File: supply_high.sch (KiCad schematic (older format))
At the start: 41 parts

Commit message: - final schematic
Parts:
- gave numbers to parts that had none: 41
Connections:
- net HVGND: now also C191.2, C192.1; no longer C191.1, C192.2
- net at C193.1, C194.1, D38.2 (A)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: now also C191.1, C192.2; no longer C191.2, C192.1
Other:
- moved on the sheet: C191, C192

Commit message: - init PCB - fix last things in schematic
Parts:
- U38: footprint (none) -> Package_SO:SOP-8_3.9x4.9mm_P1.27mm
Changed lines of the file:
@@
 F 0 "U38" H 4250 5567 50  0000 C CNN
 F 1 "TC7660S" H 4250 5476 50  0000 C CNN
-F 2 "" H 4350 5050 50  0001 C CNN
+F 2 "Package_SO:SOP-8_3.9x4.9mm_P1.27mm" H 4350 5050 50  0001 C CNN
 F 3 "http://datasheets.maximintegrated.com/en/ds/ICL7660-MAX1044.pdf" H 4350 5050 50  0001 C CNN
 	1    4250 5150
@@
 Wire Wire Line
 	5150 4750 4850 4750
+$Comp
+L power:PWR_FLAG #FLG?
+U 1 1 5FA95447
+P 3400 4600
+AR Path="/5F61C123/5FA95447" Ref="#FLG?"  Part="1"
+AR Path="/5FB035A9/5FA95447" Ref="#FLG0111"  Part="1"
+F 0 "#FLG0111" H 3400 4675 50  0001 C CNN
+F 1 "PWR_FLAG" H 3400 4774 50  0001 C CNN
+F 2 "" H 3400 4600 50  0001 C CNN
+F 3 "~" H 3400 4600 50  0001 C CNN
+	1    3400 4600
+	1    0    0    -1
+$EndComp
 $EndSCHEMATC

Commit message: - PCB progress
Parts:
- C177, C179, C181, C182, C183, C185, C186, C187, C188, C189, C190, C191, C194, C195, C197: footprint Capacitor_SMD:C_0603_1608Metric_Pad1.05x0.95mm_HandSolder -> Capacitor_SMD:C_0603_1608Metric
- C178, C180, C193, C196: footprint Capacitor_SMD:C_0805_2012Metric_Pad1.15x1.40mm_HandSolder -> Capacitor_SMD:C_0805_2012Metric
- C184, C192, C198: footprint Capacitor_SMD:C_0805_2012Metric_Pad1.15x1.40mm_HandSolder -> Capacitor_SMD:C_0603_1608Metric_Pad1.05x0.95mm_HandSolder
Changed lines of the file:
@@
 F 0 "C188" H 3400 4650 50  0000 R BNN
 F 1 "100n" H 3400 4850 50  0000 R TNN
-F 2 "Capacitor_SMD:C_0603_1608Metric_Pad1.05x0.95mm_HandSolder" H 3400 4750 50  0001 C CNN
+F 2 "Capacitor_SMD:C_0603_1608Metric" H 3400 4750 50  0001 C CNN
 F 3 "~" H 3400 4750 50  0001 C CNN
 	1    3400 4750
@@
 F 0 "C183" H 6850 2750 50  0000 L BNN
 F 1 "10n" H 6850 2650 50  0000 L TNN
-F 2 "Capacitor_SMD:C_0603_1608Metric_Pad1.05x0.95mm_HandSolder" H 6800 2700 50  0001 C CNN
+F 2 "Capacitor_SMD:C_0603_1608Metric" H 6800 2700 50  0001 C CNN
 F 3 "~" H 6800 2700 50  0001 C CNN
 	1    6800 2700
@@
 F 0 "C182" H 5800 2750 50  0000 L BNN
 F 1 "100n" H 5800 2650 50  0000 L TNN
-F 2 "Capacitor_SMD:C_0603_1608Metric_Pad1.05x0.95mm_HandSolder" H 5750 2700 50  0001 C CNN
+F 2 "Capacitor_SMD:C_0603_1608Metric" H 5750 2700 50  0001 C CNN
 F 3 "~" H 5750 2700 50  0001 C CNN
 	1    5750 2700
@@
 F 0 "C181" H 5500 2750 50  0000 L BNN
 F 1 "1u" H 5500 2650 50  0000 L TNN
-F 2 "Capacitor_SMD:C_0603_1608Metric_Pad1.05x0.95mm_HandSolder" H 5450 2700 50  0001 C CNN
+F 2 "Capacitor_SMD:C_0603_1608Metric" H 5450 2700 50  0001 C CNN
 F 3 "~" H 5450 2700 50  0001 C CNN
 	1    5450 2700
@@
 F 0 "C184" H 7150 2750 50  0000 L BNN
 F 1 "10u" H 7150 2650 50  0000 L TNN
-F 2 "Capacitor_SMD:C_0805_2012Metric_Pad1.15x1.40mm_HandSolder" H 7100 2700 50  0001 C CNN
+F 2 "Capacitor_SMD:C_0603_1608Metric_Pad1.05x0.95mm_HandSolder" H 7100 2700 50  0001 C CNN
 F 3 "Samsung CL21A106KQFNNNE" H 7100 2700 50  0001 C CNN
 	1    7100 2700
@@
 F 0 "C186" H 7750 2750 50  0000 L BNN
 F 1 "100n" H 7750 2650 50  0000 L TNN
-F 2 "Capacitor_SMD:C_0603_1608Metric_Pad1.05x0.95mm_HandSolder" H 7700 2700 50  0001 C CNN
+F 2 "Capacitor_SMD:C_0603_1608Metric" H 7700 2700 50  0001 C CNN
 F 3 "~" H 7700 2700 50  0001 C CNN
 	1    7700 2700
@@
 F 0 "C185" H 7450 2750 50  0000 L BNN
 F 1 "1u" H 7450 2650 50  0000 L TNN
-F 2 "Capacitor_SMD:C_0603_1608Metric_Pad1.05x0.95mm_HandSolder" H 7400 2700 50  0001 C CNN
+F 2 "Capacitor_SMD:C_0603_1608Metric" H 7400 2700 50  0001 C CNN
 F 3 "~" H 7400 2700 50  0001 C CNN
 	1    7400 2700
@@
 F 0 "C198" H 3650 5300 50  0000 L BNN
 F 1 "10u" H 3650 5200 50  0000 L TNN
-F 2 "Capacitor_SMD:C_0805_2012Metric_Pad1.15x1.40mm_HandSolder" H 3600 5250 50  0001 C CNN
+F 2 "Capacitor_SMD:C_0603_1608Metric_Pad1.05x0.95mm_HandSolder" H 3600 5250 50  0001 C CNN
 F 3 "Samsung CL21A106KQFNNNE" H 3600 5250 50  0001 C CNN
 	1    3600 5250
@@
 F 0 "C197" H 3350 5300 50  0000 L BNN
 F 1 "100n" H 3350 5200 50  0000 L TNN
-F 2 "Capacitor_SMD:C_0603_1608Metric_Pad1.05x0.95mm_HandSolder" H 3300 5250 50  0001 C CNN
+F 2 "Capacitor_SMD:C_0603_1608Metric" H 3300 5250 50  0001 C CNN
 F 3 "~" H 3300 5250 50  0001 C CNN
 	1    3300 5250
@@
 F 0 "C192" H 5500 5000 50  0000 L BNN
 F 1 "10u" H 5500 4900 50  0000 L TNN
-F 2 "Capacitor_SMD:C_0805_2012Metric_Pad1.15x1.40mm_HandSolder" H 5450 4950 50  0001 C CNN
+F 2 "Capacitor_SMD:C_0603_1608Metric_Pad1.05x0.95mm_HandSolder" H 5450 4950 50  0001 C CNN
 F 3 "Samsung CL21A106KQFNNNE" H 5450 4950 50  0001 C CNN
 	1    5450 4950
@@
 F 0 "C190" H 4850 4850 50  0000 R BNN
 F 1 "100n" H 4850 5050 50  0000 R TNN
-F 2 "Capacitor_SMD:C_0603_1608Metric_Pad1.05x0.95mm_HandSolder" H 4850 4950 50  0001 C CNN
+F 2 "Capacitor_SMD:C_0603_1608Metric" H 4850 4950 50  0001 C CNN
 F 3 "~" H 4850 4950 50  0001 C CNN
 	1    4850 4950
@@
 F 0 "C191" H 5150 4850 50  0000 R BNN
 F 1 "100n" H 5150 5050 50  0000 R TNN
-F 2 "Capacitor_SMD:C_0603_1608Metric_Pad1.05x0.95mm_HandSolder" H 5150 4950 50  0001 C CNN
+F 2 "Capacitor_SMD:C_0603_1608Metric" H 5150 4950 50  0001 C CNN
 F 3 "~" H 5150 4950 50  0001 C CNN
 	1    5150 4950
@@
 F 0 "C193" H 5900 5050 50  0000 L BNN
 F 1 "2u2" H 5900 4950 50  0000 L TNN
-F 2 "Capacitor_SMD:C_0805_2012Metric_Pad1.15x1.40mm_HandSolder" H 5850 5000 50  0001 C CNN
+F 2 "Capacitor_SMD:C_0805_2012Metric" H 5850 5000 50  0001 C CNN
 F 3 "~" H 5850 5000 50  0001 C CNN
 	1    5850 5000
@@
 F 0 "C194" H 6250 5050 50  0000 L BNN
 F 1 "100n" H 6250 4950 50  0000 L TNN
-F 2 "Capacitor_SMD:C_0603_1608Metric_Pad1.05x0.95mm_HandSolder" H 6200 5000 50  0001 C CNN
+F 2 "Capacitor_SMD:C_0603_1608Metric" H 6200 5000 50  0001 C CNN
 F 3 "~" H 6200 5000 50  0001 C CNN
 	1    6200 5000
@@
 F 0 "C196" H 8250 5050 50  0000 L BNN
 F 1 "2u2" H 8250 4950 50  0000 L TNN
-F 2 "Capacitor_SMD:C_0805_2012Metric_Pad1.15x1.40mm_HandSolder" H 8200 5000 50  0001 C CNN
+F 2 "Capacitor_SMD:C_0805_2012Metric" H 8200 5000 50  0001 C CNN
 F 3 "~" H 8200 5000 50  0001 C CNN
 	1    8200 5000
@@
 F 0 "C195" H 7900 5050 50  0000 L BNN
 F 1 "100n" H 7900 4950 50  0000 L TNN
-F 2 "Capacitor_SMD:C_0603_1608Metric_Pad1.05x0.95mm_HandSolder" H 7850 5000 50  0001 C CNN
+F 2 "Capacitor_SMD:C_0603_1608Metric" H 7850 5000 50  0001 C CNN
 F 3 "~" H 7850 5000 50  0001 C CNN
 	1    7850 5000
@@
 F 0 "C189" H 7050 4900 50  0000 L BNN
 F 1 "1u" H 7050 4800 50  0000 L TNN
-F 2 "Capacitor_SMD:C_0603_1608Metric_Pad1.05x0.95mm_HandSolder" H 7000 4850 50  0001 C CNN
+F 2 "Capacitor_SMD:C_0603_1608Metric" H 7000 4850 50  0001 C CNN
 F 3 "~" H 7000 4850 50  0001 C CNN
 	1    7000 4850
@@
 F 0 "C180" H 4850 2750 50  0000 L BNN
 F 1 "2u2" H 4850 2650 50  0000 L TNN
-F 2 "Capacitor_SMD:C_0805_2012Metric_Pad1.15x1.40mm_HandSolder" H 4800 2700 50  0001 C CNN
+F 2 "Capacitor_SMD:C_0805_2012Metric" H 4800 2700 50  0001 C CNN
 F 3 "~" H 4800 2700 50  0001 C CNN
 	1    4800 2700
@@
 F 0 "C179" H 4500 2750 50  0000 L BNN
 F 1 "100n" H 4500 2650 50  0000 L TNN
-F 2 "Capacitor_SMD:C_0603_1608Metric_Pad1.05x0.95mm_HandSolder" H 4450 2700 50  0001 C CNN
+F 2 "Capacitor_SMD:C_0603_1608Metric" H 4450 2700 50  0001 C CNN
 F 3 "~" H 4450 2700 50  0001 C CNN
 	1    4450 2700
@@
 F 0 "C187" H 3850 3000 50  0000 L BNN
 F 1 "1u" H 3850 2900 50  0000 L TNN
-F 2 "Capacitor_SMD:C_0603_1608Metric_Pad1.05x0.95mm_HandSolder" H 3800 2950 50  0001 C CNN
+F 2 "Capacitor_SMD:C_0603_1608Metric" H 3800 2950 50  0001 C CNN
 F 3 "~" H 3800 2950 50  0001 C CNN
 	1    3800 2950
@@
 F 0 "C178" H 3000 2750 50  0000 L BNN
 F 1 "2u2" H 3000 2650 50  0000 L TNN
-F 2 "Capacitor_SMD:C_0805_2012Metric_Pad1.15x1.40mm_HandSolder" H 2950 2700 50  0001 C CNN
+F 2 "Capacitor_SMD:C_0805_2012Metric" H 2950 2700 50  0001 C CNN
 F 3 "~" H 2950 2700 50  0001 C CNN
 	1    2950 2700
@@
 F 0 "C177" H 2700 2750 50  0000 L BNN
 F 1 "100n" H 2700 2650 50  0000 L TNN
-F 2 "Capacitor_SMD:C_0603_1608Metric_Pad1.05x0.95mm_HandSolder" H 2650 2700 50  0001 C CNN
+F 2 "Capacitor_SMD:C_0603_1608Metric" H 2650 2700 50  0001 C CNN
 F 3 "~" H 2650 2700 50  0001 C CNN
 	1    2650 2700

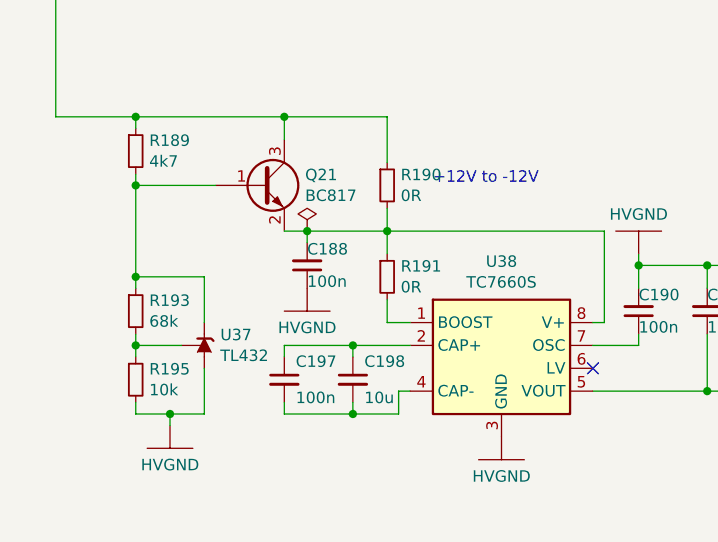
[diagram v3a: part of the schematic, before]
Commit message: - PCB WiP - Pump output aligned
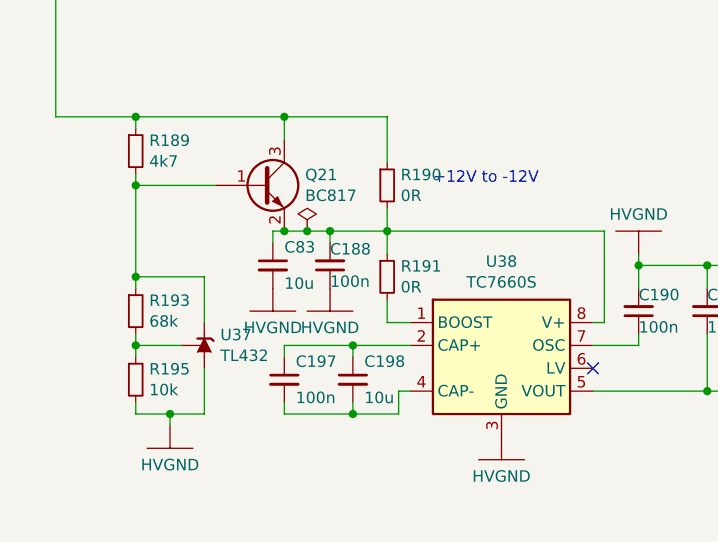
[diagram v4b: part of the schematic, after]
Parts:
- added C83: 10u, Capacitor_SMD:C_0603_1608Metric_Pad1.05x0.95mm_HandSolder, symbol Device:C_Small
- R189, R190, R191: footprint Resistor_SMD:R_0603_1608Metric_Pad1.05x0.95mm_HandSolder -> Resistor_SMD:R_0603_1608Metric
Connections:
- net HVGND: now also C83.2
- net at C188.2, Q21.2 (E), R190.2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: now also C83.1
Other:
- moved on the sheet: C188
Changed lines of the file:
@@
 L Device:C_Small C?
 U 1 1 5FB2240D
-P 3400 4750
+P 3500 4750
 AR Path="/5F40DCB9/5FB2240D" Ref="C?"  Part="1"
 AR Path="/5F463F4C/5FB2240D" Ref="C?"  Part="1"
@@
 AR Path="/5F61C123/5FB2240D" Ref="C?"  Part="1"
 AR Path="/5FB035A9/5FB2240D" Ref="C188"  Part="1"
-F 0 "C188" H 3400 4650 50  0000 R BNN
-F 1 "100n" H 3400 4850 50  0000 R TNN
-F 2 "Capacitor_SMD:C_0603_1608Metric" H 3400 4750 50  0001 C CNN
-F 3 "~" H 3400 4750 50  0001 C CNN
-	1    3400 4750
+F 0 "C188" H 3500 4650 50  0000 R BNN
+F 1 "100n" H 3500 4850 50  0000 R TNN
+F 2 "Capacitor_SMD:C_0603_1608Metric" H 3500 4750 50  0001 C CNN
+F 3 "~" H 3500 4750 50  0001 C CNN
+	1    3500 4750
 	-1   0    0    1
 $EndComp
@@
 F 0 "R191" H 3809 4846 50  0000 L CNN
 F 1 "0R" H 3809 4755 50  0000 L CNN
-F 2 "Resistor_SMD:R_0603_1608Metric_Pad1.05x0.95mm_HandSolder" H 3750 4800 50  0001 C CNN
+F 2 "Resistor_SMD:R_0603_1608Metric" H 3750 4800 50  0001 C CNN
 F 3 "~" H 3750 4800 50  0001 C CNN
 	1    3750 4800
@@
 F 0 "R189" H 2709 4296 50  0000 L CNN
 F 1 "4k7" H 2709 4205 50  0000 L CNN
-F 2 "Resistor_SMD:R_0603_1608Metric_Pad1.05x0.95mm_HandSolder" H 2650 4250 50  0001 C CNN
+F 2 "Resistor_SMD:R_0603_1608Metric" H 2650 4250 50  0001 C CNN
 F 3 "~" H 2650 4250 50  0001 C CNN
 	1    2650 4250
@@
 F 0 "R190" H 3809 4446 50  0000 L CNN
 F 1 "0R" H 3809 4355 50  0000 L CNN
-F 2 "Resistor_SMD:R_0603_1608Metric_Pad1.05x0.95mm_HandSolder" H 3750 4400 50  0001 C CNN
+F 2 "Resistor_SMD:R_0603_1608Metric" H 3750 4400 50  0001 C CNN
 F 3 "~" H 3750 4400 50  0001 C CNN
 	1    3750 4400
@@
 L power_my:HVGND #PWR?
 U 1 1 5FB44224
-P 3400 4850
+P 3500 4850
 AR Path="/5FB44224" Ref="#PWR?"  Part="1"
 AR Path="/5FB035A9/5FB44224" Ref="#PWR0244"  Part="1"
-F 0 "#PWR0244" H 3400 4800 50  0001 C CNN
-F 1 "HVGND" H 3400 4677 50  0000 C CNN
-F 2 "" H 3400 4850 50  0001 C CNN
-F 3 "" H 3400 4850 50  0001 C CNN
-	1    3400 4850
-	1    0    0    -1
-$EndComp
-Wire Wire Line
-	3750 4600 3400 4600
+F 0 "#PWR0244" H 3500 4800 50  0001 C CNN
+F 1 "HVGND" H 3500 4677 50  0000 C CNN
+F 2 "" H 3500 4850 50  0001 C CNN
+F 3 "" H 3500 4850 50  0001 C CNN
+	1    3500 4850
+	1    0    0    -1
+$EndComp
+Wire Wire Line
+	3750 4600 3500 4600
 Connection ~ 3750 4600
-Wire Wire Line
-	3400 4650 3400 4600
 Connection ~ 3400 4600
 Wire Wire Line
@@
 	1    0    0    -1
 $EndComp
+$Comp
+L Device:C_Small C?
+U 1 1 5FAA7ACF
+P 3250 4750
+AR Path="/5F620813/5FAA7ACF" Ref="C?"  Part="1"
+AR Path="/5F7A93EE/5FAA7ACF" Ref="C?"  Part="1"
+AR Path="/5FB035A9/5FAA7ACF" Ref="C83"  Part="1"
+F 0 "C83" H 3300 4800 50  0000 L BNN
+F 1 "10u" H 3300 4700 50  0000 L TNN
+F 2 "Capacitor_SMD:C_0603_1608Metric_Pad1.05x0.95mm_HandSolder" H 3250 4750 50  0001 C CNN
+F 3 "Samsung CL21A106KQFNNNE" H 3250 4750 50  0001 C CNN
+	1    3250 4750
+	1    0    0    -1
+$EndComp
+$Comp
+L power_my:HVGND #PWR?
+U 1 1 5FAADF04
+P 3250 4850
+AR Path="/5FAADF04" Ref="#PWR?"  Part="1"
+AR Path="/5FB035A9/5FAADF04" Ref="#PWR087"  Part="1"
+F 0 "#PWR087" H 3250 4800 50  0001 C CNN
+F 1 "HVGND" H 3250 4677 50  0000 C CNN
+F 2 "" H 3250 4850 50  0001 C CNN
+F 3 "" H 3250 4850 50  0001 C CNN
+	1    3250 4850
+	1    0    0    -1
+$EndComp
+Wire Wire Line
+	3250 4650 3250 4600
+Wire Wire Line
+	3250 4600 3300 4600
+Connection ~ 3300 4600
+Wire Wire Line
+	3500 4650 3500 4600
+Connection ~ 3500 4600
+Wire Wire Line
+	3500 4600 3400 4600
 $EndSCHEMATC

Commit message: - PCB WiP
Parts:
- removed C186: 100n, Capacitor_SMD:C_0603_1608Metric, symbol Device:C_Small
- removed C193: 2u2, Capacitor_SMD:C_0805_2012Metric, symbol Device:C_Small
- added D13: 1N4448, miscellaneous_my:D_SOD-323-523_HandSoldering, symbol Device:D_Small
- D35, D36, D37, D38: footprint Diode_SMD:D_SOD-323_HandSoldering -> miscellaneous_my:D_SOD-323-523_HandSoldering
- U38: footprint Package_SO:SOP-8_3.9x4.9mm_P1.27mm -> Package_SO:SOIC-8_3.9x4.9mm_P1.27mm
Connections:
- net HV+3V3: now also D13.2 (A)
- net HV+5V: now also D13.1 (K)
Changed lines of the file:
@@
 $Descr A4 11693 8268
 encoding utf-8
-Sheet 11 11
+Sheet 11 10
 Title ""
 Date ""
@@
 F 0 "U38" H 4250 5567 50  0000 C CNN
 F 1 "TC7660S" H 4250 5476 50  0000 C CNN
-F 2 "Package_SO:SOP-8_3.9x4.9mm_P1.27mm" H 4350 5050 50  0001 C CNN
+F 2 "Package_SO:SOIC-8_3.9x4.9mm_P1.27mm" H 4350 5050 50  0001 C CNN
 F 3 "http://datasheets.maximintegrated.com/en/ds/ICL7660-MAX1044.pdf" H 4350 5050 50  0001 C CNN
 	1    4250 5150
@@
 Wire Wire Line
 	7400 2500 7400 2600
-Wire Wire Line
-	7700 2600 7700 2500
-$Comp
-L Device:C_Small C?
-U 1 1 5FB2D55D
-P 7700 2700
-AR Path="/5F620813/5FB2D55D" Ref="C?"  Part="1"
-AR Path="/5FB035A9/5FB2D55D" Ref="C186"  Part="1"
-F 0 "C186" H 7750 2750 50  0000 L BNN
-F 1 "100n" H 7750 2650 50  0000 L TNN
-F 2 "Capacitor_SMD:C_0603_1608Metric" H 7700 2700 50  0001 C CNN
-F 3 "~" H 7700 2700 50  0001 C CNN
-	1    7700 2700
-	1    0    0    -1
-$EndComp
 $Comp
 L Device:C_Small C?
@@
 Connection ~ 7400 2500
 Wire Wire Line
-	7400 2500 7700 2500
-Wire Wire Line
-	7700 2500 7700 2450
-Connection ~ 7700 2500
+	7400 2500 7400 2450
 $Comp
 L Device:C_Small C?
@@
 L power_my:HVGND #PWR?
 U 1 1 5FB3856A
-P 4850 4700
+P 4850 4650
 AR Path="/5FB3856A" Ref="#PWR?"  Part="1"
 AR Path="/5FB035A9/5FB3856A" Ref="#PWR0242"  Part="1"
-F 0 "#PWR0242" H 4850 4650 50  0001 C CNN
-F 1 "HVGND" H 4850 4527 50  0000 C CNN
-F 2 "" H 4850 4700 50  0001 C CNN
-F 3 "" H 4850 4700 50  0001 C CNN
-	1    4850 4700
+F 0 "#PWR0242" H 4850 4600 50  0001 C CNN
+F 1 "HVGND" H 4850 4477 50  0000 C CNN
+F 2 "" H 4850 4650 50  0001 C CNN
+F 3 "" H 4850 4650 50  0001 C CNN
+	1    4850 4650
 	-1   0    0    1
 $EndComp
@@
 $Comp
 L Device:C_Small C?
-U 1 1 5FB5BC8C
-P 5850 5000
-AR Path="/5F620813/5FB5BC8C" Ref="C?"  Part="1"
-AR Path="/5F7A93EE/5FB5BC8C" Ref="C?"  Part="1"
-AR Path="/5FB035A9/5FB5BC8C" Ref="C193"  Part="1"
-F 0 "C193" H 5900 5050 50  0000 L BNN
-F 1 "2u2" H 5900 4950 50  0000 L TNN
-F 2 "Capacitor_SMD:C_0805_2012Metric" H 5850 5000 50  0001 C CNN
-F 3 "~" H 5850 5000 50  0001 C CNN
-	1    5850 5000
-	-1   0    0    1
-$EndComp
-Wire Wire Line
-	5850 5100 5850 5300
-$Comp
-L Device:C_Small C?
 U 1 1 5FB5BCA6
 P 6200 5000
@@
 	-1   0    0    1
 $EndComp
-Wire Wire Line
-	5850 5300 6200 5300
 Wire Wire Line
 	6200 5100 6200 5300
@@
 F 0 "D38" H 6600 5800 50  0000 C BNN
 F 1 "1N4448" H 6600 5750 50  0000 C CNN
-F 2 "Diode_SMD:D_SOD-323_HandSoldering" V 6600 5650 50  0001 C CNN
+F 2 "miscellaneous_my:D_SOD-323-523_HandSoldering" V 6600 5650 50  0001 C CNN
 F 3 "~" V 6600 5650 50  0001 C CNN
 	1    6600 5650
@@
 F 0 "D37" V 6954 5220 50  0000 L CNN
 F 1 "1N4448" H 7000 5050 50  0000 C CNN
-F 2 "Diode_SMD:D_SOD-323_HandSoldering" V 7000 5150 50  0001 C CNN
+F 2 "miscellaneous_my:D_SOD-323-523_HandSoldering" V 7000 5150 50  0001 C CNN
 F 3 "~" V 7000 5150 50  0001 C CNN
 	1    7000 5150
@@
 	6300 5300 6200 5300
 Connection ~ 7300 5300
-Connection ~ 5850 5300
 $Comp
 L power_my:HVGND #PWR?
@@
 	7000 4700 6200 4700
 Wire Wire Line
-	5850 4700 5850 4900
-Wire Wire Line
 	6200 4900 6200 4700
-Connection ~ 6200 4700
-Wire Wire Line
-	6200 4700 5850 4700
 Text Notes 3950 4400 0    50   ~ 0
 +12V to -12V
@@
 L power_my:HV+3V3 #PWR0239
 U 1 1 5FB7E4C4
-P 7700 2450
-F 0 "#PWR0239" H 7700 2300 50  0001 C CNN
-F 1 "HV+3V3" H 7705 2623 50  0000 C CNN
-F 2 "" H 7700 2450 50  0001 C CNN
-F 3 "" H 7700 2450 50  0001 C CNN
-	1    7700 2450
+P 7400 2450
+F 0 "#PWR0239" H 7400 2300 50  0001 C CNN
+F 1 "HV+3V3" H 7405 2623 50  0000 C CNN
+F 2 "" H 7400 2450 50  0001 C CNN
+F 3 "" H 7400 2450 50  0001 C CNN
+	1    7400 2450
 	1    0    0    -1
 $EndComp
@@
 F 0 "D35" H 3400 2300 50  0000 C BNN
 F 1 "1N4448" H 3400 2250 50  0000 C CNN
-F 2 "Diode_SMD:D_SOD-323_HandSoldering" V 3400 2150 50  0001 C CNN
+F 2 "miscellaneous_my:D_SOD-323-523_HandSoldering" V 3400 2150 50  0001 C CNN
 F 3 "~" V 3400 2150 50  0001 C CNN
 	1    3400 2150
@@
 F 0 "D36" V 3750 2700 50  0000 L BNN
 F 1 "1N4448" H 3800 2550 50  0000 C CNN
-F 2 "Diode_SMD:D_SOD-323_HandSoldering" V 3800 2650 50  0001 C CNN
+F 2 "miscellaneous_my:D_SOD-323-523_HandSoldering" V 3800 2650 50  0001 C CNN
 F 3 "~" V 3800 2650 50  0001 C CNN
 	1    3800 2650
@@
 	5450 2950 5750 2950
 Wire Wire Line
-	7700 2950 7700 2800
-Connection ~ 7400 2950
-Wire Wire Line
-	7400 2950 7700 2950
-Wire Wire Line
 	7400 2800 7400 2950
 Wire Wire Line
@@
 Text Notes 4200 2150 0    50   ~ 0
 +12V to +5V
-Text Notes 6100 2150 0    50   ~ 0
+Text Notes 6150 1900 0    50   ~ 0
 +5V to +3V3
 Wire Wire Line
@@
 Connection ~ 5450 5300
 Wire Wire Line
-	5450 5300 5850 5300
-Wire Wire Line
-	4850 4700 4850 4750
-Wire Wire Line
-	5450 4850 5450 4750
-Wire Wire Line
-	5450 4750 5150 4750
-Connection ~ 4850 4750
-Wire Wire Line
-	4850 4750 4850 4850
-Wire Wire Line
-	5150 4850 5150 4750
-Connection ~ 5150 4750
-Wire Wire Line
-	5150 4750 4850 4750
+	4850 4650 4850 4700
+Wire Wire Line
+	5450 4850 5450 4700
+Wire Wire Line
+	5450 4700 5150 4700
+Connection ~ 4850 4700
+Wire Wire Line
+	4850 4700 4850 4850
+Wire Wire Line
+	5150 4850 5150 4700
+Connection ~ 5150 4700
+Wire Wire Line
+	5150 4700 4850 4700
 $Comp
 L power:PWR_FLAG #FLG?
@@
 Wire Wire Line
 	3500 4600 3400 4600
+Wire Wire Line
+	5450 5300 6200 5300
+$Comp
+L Device:D_Small D?
+U 1 1 5FB3FF99
+P 6400 2150
+AR Path="/5F620813/5FB3FF99" Ref="D?"  Part="1"
+AR Path="/5FB035A9/5FB3FF99" Ref="D13"  Part="1"
+F 0 "D13" H 6400 2300 50  0000 C BNN
+F 1 "1N4448" H 6400 2250 50  0000 C CNN
+F 2 "miscellaneous_my:D_SOD-323-523_HandSoldering" V 6400 2150 50  0001 C CNN
+F 3 "~" V 6400 2150 50  0001 C CNN
+	1    6400 2150
+	1    0    0    -1
+$EndComp
+Wire Wire Line
+	6500 2150 6800 2150
+Wire Wire Line
+	6300 2150 6000 2150
+Wire Wire Line
+	6000 2150 6000 2500
+Wire Wire Line
+	6800 2150 6800 2500
+Connection ~ 6800 2500
 $EndSCHEMATC
